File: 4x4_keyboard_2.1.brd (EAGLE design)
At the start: 69.5 x 142.2 mm, 77 parts, among them U2 AMS1117-5.0

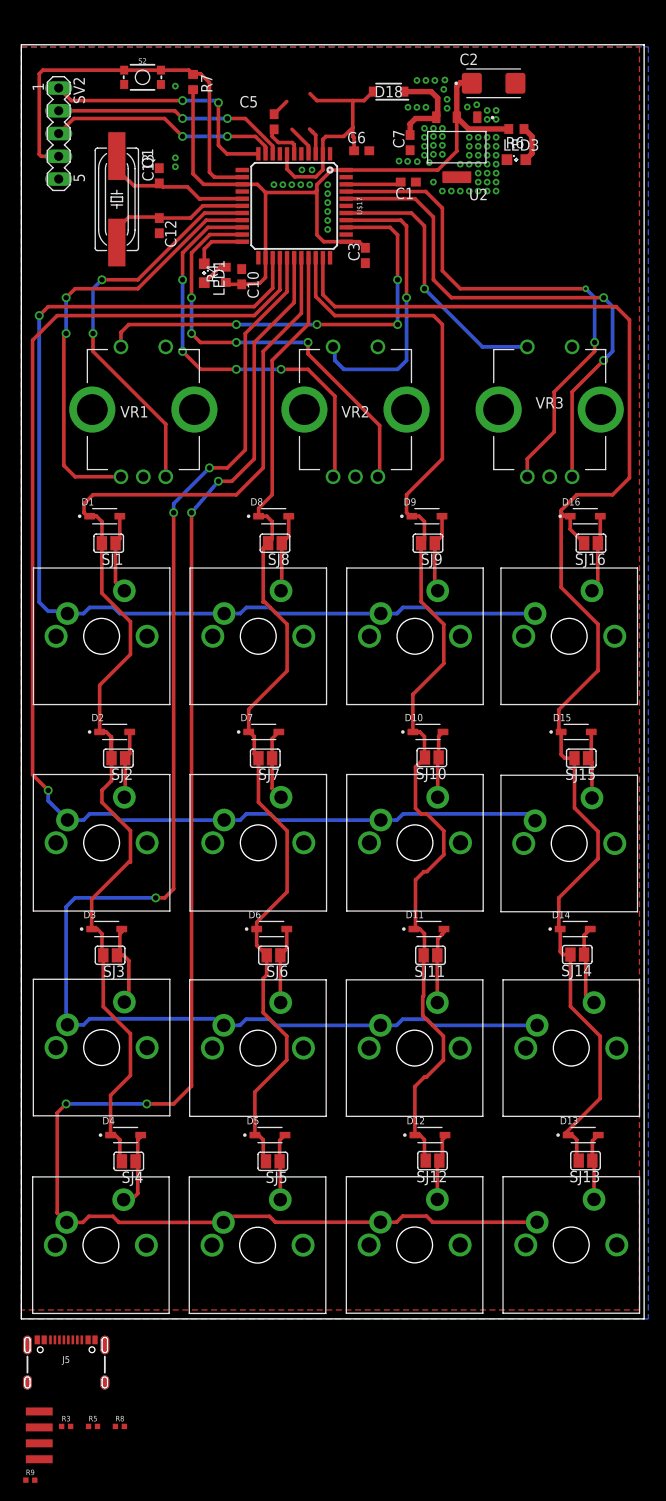
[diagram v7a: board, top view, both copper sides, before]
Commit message: change resistor package
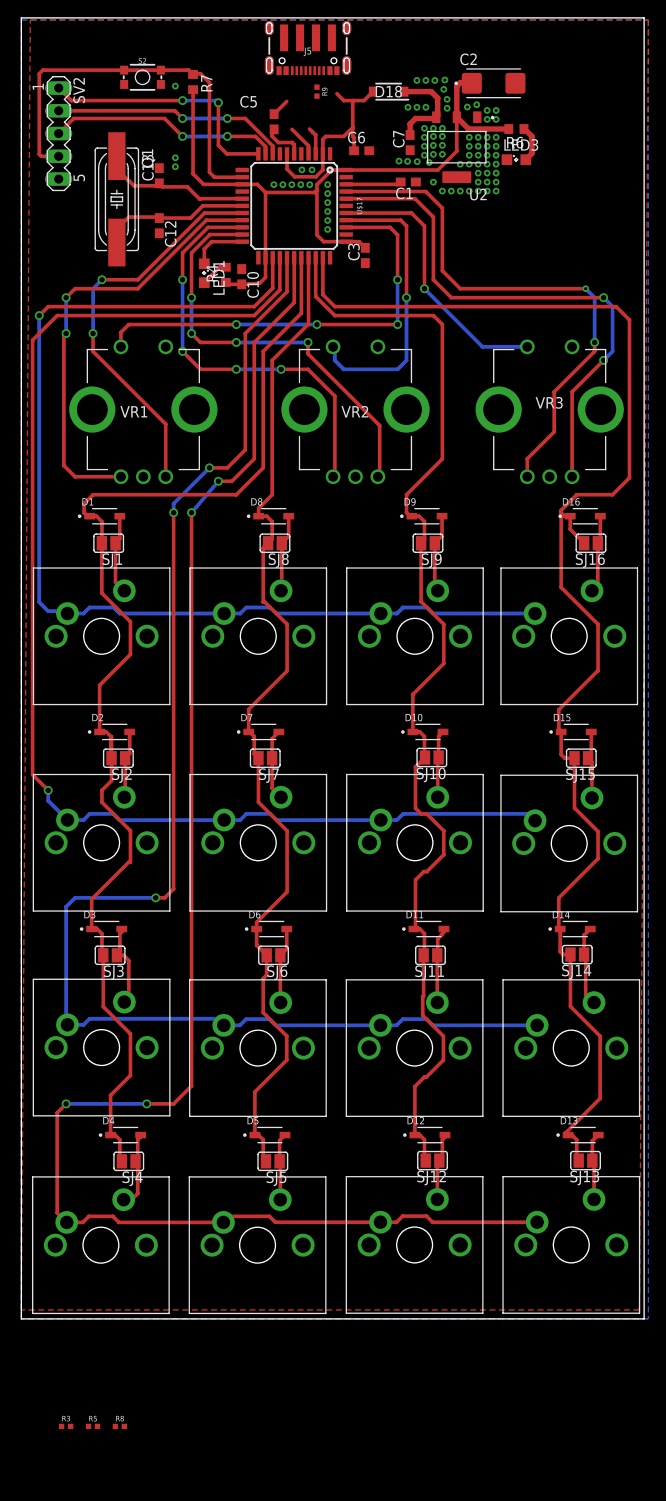
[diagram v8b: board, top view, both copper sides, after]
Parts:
- moved JP14 158.9 mm to (32.0, 143.0), turned to 270 degrees
- moved R9 158.3 mm to (33.0, 137.0), turned to 270 degrees
- moved J5 143.6 mm to (32.0, 139.0), turned to 180 degrees
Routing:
- net V_USB: track 27.1 -> 24.1 mm
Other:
- board size 69.5 x 142.2 mm -> 69.5 x 145.2 mm
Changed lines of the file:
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@@
 <?xml version="1.0" encoding="utf-8"?>
 <!DOCTYPE eagle SYSTEM "eagle.dtd">
-<eagle version="9.6.2">
+<eagle version="6.4">
 <drawing>
 <settings>
 <setting alwaysvectorfont="no"/>
-<setting keepoldvectorfont="yes"/>
 <setting verticaltext="up"/>
 </settings>
@@
 <plain>
 <wire x1="0" y1="0" x2="69.52" y2="0" width="0" layer="20"/>
-<wire x1="69.52" y1="0" x2="69.52" y2="142.23" width="0" layer="20"/>
-<wire x1="69.52" y1="142.23" x2="0" y2="142.23" width="0" layer="20"/>
-<wire x1="0" y1="142.23" x2="0" y2="0" width="0" layer="20"/>
+<wire x1="69.52" y1="0" x2="69.52" y2="145.23" width="0" layer="20"/>
+<wire x1="69.52" y1="145.23" x2="0" y2="145.23" width="0" layer="20"/>
+<wire x1="0" y1="145.23" x2="0" y2="0" width="0" layer="20"/>
 </plain>
 <attributes>
@@
 <param name="dpMaxLengthDifference" value="10mm"/>
 <param name="dpGapFactor" value="2.5"/>
+<param name="checkGrid" value="0"/>
 <param name="checkAngle" value="0"/>
 <param name="checkFont" value="1"/>
 <param name="checkRestrict" value="1"/>
-<param name="checkStop" value="0"/>
-<param name="checkValues" value="0"/>
-<param name="checkNames" value="1"/>
-<param name="checkWireStubs" value="1"/>
-<param name="checkPolygonWidth" value="0"/>
 <param name="useDiameter" value="13"/>
 <param name="maxErrors" value="50"/>
@@
 <pass name="Default">
 <param name="RoutingGrid" value="50mil"/>
-<param name="AutoGrid" value="1"/>
-<param name="Efforts" value="0"/>
-<param name="TopRouterVariant" value="1"/>
 <param name="tpViaShape" value="round"/>
 <param name="PrefDir.1" value="|"/>
@@
 <attribute name="VALUE" x="11" y="-12.562" size="0.6096" layer="27" font="vector" ratio="20" align="top-center"/>
 </element>
-<element name="R9" library="SparkFun-Resistors" package="0402-TIGHT" value="5.1k" x="1" y="-18" smashed="yes">
-<attribute name="NAME" x="1" y="-17.438" size="0.6096" layer="25" font="vector" ratio="20" align="bottom-center"/>
-<attribute name="PROD_ID" value="RES-14340" x="2" y="-11" size="1.778" layer="27" display="off"/>
-<attribute name="VALUE" x="1" y="-18.562" size="0.6096" layer="27" font="vector" ratio="20" align="top-center"/>
-</element>
-<element name="JP14" library="SparkFun-Connectors" package="USB-SOLDER-PADS" value="USB_SOLDER_PADS" x="2" y="-13" smashed="yes"/>
-<element name="J5" library="USBC" package="USB-C-16P-5" value="" x="5" y="-2" smashed="yes">
-<attribute name="NAME" x="5" y="-4.54" size="0.762" layer="25" align="center"/>
-<attribute name="VALUE" x="5" y="-5.81" size="0.762" layer="27" align="center"/>
+<element name="R9" library="SparkFun-Resistors" package="0402-TIGHT" value="5.1k" x="33" y="137" smashed="yes" rot="R270">
+<attribute name="NAME" x="33.562" y="137" size="0.6096" layer="25" font="vector" ratio="20" rot="R270" align="bottom-center"/>
+<attribute name="PROD_ID" value="RES-14340" x="40" y="136" size="1.778" layer="27" rot="R270" display="off"/>
+<attribute name="VALUE" x="32.438" y="137" size="0.6096" layer="27" font="vector" ratio="20" rot="R270" align="top-center"/>
+</element>
+<element name="JP14" library="SparkFun-Connectors" package="USB-SOLDER-PADS" value="USB_SOLDER_PADS" x="32" y="143" smashed="yes" rot="R270"/>
+<element name="J5" library="USBC" package="USB-C-16P-5" value="" x="32" y="139" smashed="yes" rot="R180">
+<attribute name="NAME" x="32" y="141.54" size="0.762" layer="25" rot="R180" align="center"/>
+<attribute name="VALUE" x="32" y="142.81" size="0.762" layer="27" rot="R180" align="center"/>
 </element>
 </elements>
@@
 <contactref element="C2" pad="2"/>
 <polygon width="0.4064" layer="1" isolate="0.254" orphans="yes" thermals="no">
-<vertex x="0" y="142"/>
-<vertex x="69" y="142"/>
+<vertex x="1" y="145"/>
+<vertex x="70" y="145"/>
 <vertex x="69" y="1"/>
 <vertex x="0" y="1"/>
 </polygon>
 <polygon width="0.4064" layer="16">
-<vertex x="0" y="142"/>
-<vertex x="70" y="142"/>
+<vertex x="0" y="145"/>
+<vertex x="70" y="145"/>
 <vertex x="70" y="0"/>
 <vertex x="0" y="0"/>
@@
 <wire x1="61.48" y1="108.51" x2="53" y2="125.9" width="0" layer="19" extent="1-1"/>
 <wire x1="58.98" y1="94.01" x2="61.48" y2="108.51" width="0" layer="19" extent="1-1"/>
-<wire x1="8.225" y1="-2.34" x2="13.62" y2="94.01" width="0" layer="19" extent="1-1"/>
-<wire x1="1.775" y1="-2.34" x2="8.225" y2="-2.34" width="0" layer="19" extent="1-1"/>
-<wire x1="7.5" y1="-12" x2="8.225" y2="-2.34" width="0" layer="19" extent="1-1"/>
+<wire x1="28.775" y1="139.34" x2="13.62" y2="94.01" width="0" layer="19" extent="1-1"/>
+<wire x1="35.225" y1="139.34" x2="28.775" y2="139.34" width="0" layer="19" extent="1-1"/>
+<wire x1="7.5" y1="-12" x2="28.775" y2="139.34" width="0" layer="19" extent="1-1"/>
 <wire x1="4.5" y1="-12" x2="7.5" y2="-12" width="0" layer="19" extent="1-1"/>
-<wire x1="2" y1="-15.667" x2="4.5" y2="-12" width="0" layer="19" extent="1-1"/>
+<wire x1="29.333" y1="143" x2="4.5" y2="-12" width="0" layer="19" extent="1-1"/>
 </signal>
 <signal name="D-">
@@
 <wire x1="30.21" y1="132.79" x2="32.06" y2="130.94" width="0.4064" layer="1"/>
 <contactref element="R9" pad="2"/>
-<wire x1="1.5" y1="-18" x2="32.06" y2="130.05" width="0" layer="19" extent="1-1"/>
+<wire x1="33" y1="136.5" x2="32.06" y2="130.05" width="0" layer="19" extent="1-1"/>
 </signal>
 <signal name="V_USB">
@@
 <wire x1="33.655" y1="130.045" x2="33.66" y2="130.05" width="0.4064" layer="1"/>
 <contactref element="D18" pad="2"/>
-<wire x1="32.23" y1="136.77" x2="33" y2="136" width="0.4064" layer="1"/>
-<wire x1="33" y1="136" x2="37" y2="136" width="0.4064" layer="1"/>
+<wire x1="35.23" y1="136.77" x2="36" y2="136" width="0.4064" layer="1"/>
+<wire x1="36" y1="136" x2="37" y2="136" width="0.4064" layer="1"/>
 <wire x1="37" y1="136" x2="38.25" y2="136" width="0.4064" layer="1"/>
 <wire x1="38.25" y1="136" x2="39.25" y2="137" width="0.4064" layer="1"/>
@@
 <contactref element="J5" pad="VBUS1"/>
 <contactref element="J5" pad="VBUS2"/>
-<wire x1="7.45" y1="-2.34" x2="29.66" y2="130.05" width="0" layer="19" extent="1-1"/>
-<wire x1="2.55" y1="-2.34" x2="7.45" y2="-2.34" width="0" layer="19" extent="1-1"/>
-<wire x1="2" y1="-10.333" x2="2.55" y2="-2.34" width="0" layer="19" extent="1-1"/>
+<wire x1="29.55" y1="139.34" x2="29.66" y2="130.05" width="0" layer="19" extent="1-1"/>
+<wire x1="34.45" y1="139.34" x2="29.55" y2="139.34" width="0" layer="19" extent="1-1"/>
+<wire x1="34.667" y1="143" x2="34.45" y2="139.34" width="0" layer="19" extent="1-1"/>
 </signal>
 <signal name="VCC">
@@
 <contactref element="J5" pad="B7"/>
 <contactref element="J5" pad="A7"/>
-<wire x1="10.5" y1="-12" x2="2" y2="-12.111" width="0" layer="19" extent="1-1"/>
-<wire x1="4.25" y1="-2.34" x2="2" y2="-12.111" width="0" layer="19" extent="1-1"/>
-<wire x1="5.25" y1="-2.34" x2="4.25" y2="-2.34" width="0" layer="19" extent="1-1"/>
+<wire x1="10.5" y1="-12" x2="32.889" y2="143" width="0" layer="19" extent="1-1"/>
+<wire x1="32.75" y1="139.34" x2="32.889" y2="143" width="0" layer="19" extent="1-1"/>
+<wire x1="31.75" y1="139.34" x2="32.75" y2="139.34" width="0" layer="19" extent="1-1"/>
 </signal>
 <signal name="DP_HV">
@@
 <contactref element="J5" pad="A6"/>
 <contactref element="J5" pad="B6"/>
-<wire x1="2" y1="-13.889" x2="0.5" y2="-18" width="0" layer="19" extent="1-1"/>
-<wire x1="4.75" y1="-2.34" x2="2" y2="-13.889" width="0" layer="19" extent="1-1"/>
-<wire x1="5.75" y1="-2.34" x2="4.75" y2="-2.34" width="0" layer="19" extent="1-1"/>
+<wire x1="31.111" y1="143" x2="33" y2="137.5" width="0" layer="19" extent="1-1"/>
+<wire x1="32.25" y1="139.34" x2="31.111" y2="143" width="0" layer="19" extent="1-1"/>
+<wire x1="31.25" y1="139.34" x2="32.25" y2="139.34" width="0" layer="19" extent="1-1"/>
 </signal>
 <signal name="N$7">
 <contactref element="R5" pad="2"/>
 <contactref element="J5" pad="A5"/>
-<wire x1="3.75" y1="-2.34" x2="8.5" y2="-12" width="0" layer="19" extent="1-1"/>
+<wire x1="33.25" y1="139.34" x2="8.5" y2="-12" width="0" layer="19" extent="1-1"/>
 </signal>
 <signal name="N$13">
 <contactref element="R3" pad="2"/>
 <contactref element="J5" pad="B5"/>
-<wire x1="6.75" y1="-2.34" x2="5.5" y2="-12" width="0" layer="19" extent="1-1"/>
+<wire x1="30.25" y1="139.34" x2="5.5" y2="-12" width="0" layer="19" extent="1-1"/>
 </signal>
 </signals>
-<mfgpreviewcolors>
-<mfgpreviewcolor name="soldermaskcolor" color="0xC8008000"/>
-<mfgpreviewcolor name="silkscreencolor" color="0xFFFEFEFE"/>
-<mfgpreviewcolor name="backgroundcolor" color="0xFF282828"/>
-<mfgpreviewcolor name="coppercolor" color="0xFFFFBF00"/>
-<mfgpreviewcolor name="substratecolor" color="0xFF786E46"/>
-</mfgpreviewcolors>
 </board>
 </drawing>
